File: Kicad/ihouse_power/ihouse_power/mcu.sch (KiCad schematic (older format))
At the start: 108 parts, among them J13 RJ33_Shielded, J20 Conn_02x05_Top_Bottom, J3 Conn_01x20, J4 Conn_01x20, M1 stm32f1_module, Q1 IRF7403, Q2 IRF7403, Q3 IRF7403, Q4 IRF7403, Q5 BC847, U10 MAX232, U11 L7805, U6 EL814, U7 EL814, U8 EL814, U9 24LC32

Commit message: 20190517
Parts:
- added C?: C, Capacitor_SMD:C_0805_2012Metric_Pad1.15x1.40mm_HandSolder, symbol Device:C
- added D?: D, Diode_SMD:D_MiniMELF, symbol Device:D
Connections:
- net 3VDC: now also D?.2 (A)
- net COM1: now also C?.2
- net VBAT: now also C?.1, D?.1 (K)
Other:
- moved on the sheet: BT1
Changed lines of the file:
@@
 L Device:Battery_Cell BT1
 U 1 1 5CD63D8E
-P 6150 4600
-F 0 "BT1" V 6000 4450 50  0000 L CNN
-F 1 "3V3" V 6100 4450 50  0000 L CNN
-F 2 "1220 Battery Holder:Battery_holder_1220" V 6150 4660 50  0001 C CNN
-F 3 "~" V 6150 4660 50  0001 C CNN
-	1    6150 4600
-	0    1    1    0
-$EndComp
-Wire Wire Line
-	7100 4600 6350 4600
+P 6050 4600
+F 0 "BT1" V 5900 4450 50  0000 L CNN
+F 1 "3V3" V 6000 4450 50  0000 L CNN
+F 2 "1220 Battery Holder:Battery_holder_1220" V 6050 4660 50  0001 C CNN
+F 3 "~" V 6050 4660 50  0001 C CNN
+	1    6050 4600
+	0    1    1    0
+$EndComp
 $Comp
 L Memory_EEPROM:24LC32 U9
@@
 	0    1    1    0
 $EndComp
-Wire Wire Line
-	7100 4350 6650 4350
 $Comp
 L Device:CP C11
@@
 Text HLabel 8500 5650 2    50   Output ~ 0
 ~TBCMD
-Wire Wire Line
-	7100 4450 6650 4450
 Wire Wire Line
 	7100 4850 6650 4850
@@
 Text Label 11350 4600 0    50   ~ 0
 3VDC
-Text Label 6650 4450 0    50   ~ 0
+Text Label 6800 4450 0    50   ~ 0
 3VDC
 Text Label 8350 5350 2    50   ~ 0
@@
 QCH_D3
 Wire Wire Line
-	5650 4600 6050 4600
+	5650 4600 5950 4600
 Text Label 3100 7700 2    50   ~ 0
 OPTIC_AI
@@
 Wire Wire Line
 	4250 2350 4350 2350
-Text HLabel 6650 4350 0    50   Output ~ 0
-3VDC
 $Comp
 L Connector:RJ33_Shielded J13
@@
 Text Notes 10300 9200 0    50   ~ 0
 PWM1 - WC duru pasvietimas\nPWM2 - vonios duru pasvietimas
+Text HLabel 5850 4350 0    50   Output ~ 0
+3VDC
+Wire Wire Line
+	7100 4600 6300 4600
+Wire Wire Line
+	6400 4450 6300 4450
+Wire Wire Line
+	6300 4450 6300 4600
+Connection ~ 6300 4600
+Wire Wire Line
+	6300 4600 6250 4600
+Wire Wire Line
+	5850 4350 7100 4350
+Wire Wire Line
+	7100 4450 6700 4450
+$Comp
+L Device:D D?
+U 1 1 5CEB3D8E
+P 6550 4450
+F 0 "D?" H 6500 4600 50  0000 L CNN
+F 1 "D" H 6350 4600 50  0000 L CNN
+F 2 "Diode_SMD:D_MiniMELF" H 6550 4450 50  0001 C CNN
+F 3 "~" H 6550 4450 50  0001 C CNN
+	1    6550 4450
+	1    0    0    -1
+$EndComp
+$Comp
+L Device:C C?
+U 1 1 5D3B6207
+P 6300 4850
+F 0 "C?" H 6000 4900 50  0000 L CNN
+F 1 "C" H 6000 4800 50  0000 L CNN
+F 2 "Capacitor_SMD:C_0805_2012Metric_Pad1.15x1.40mm_HandSolder" H 6338 4700 50  0001 C CNN
+F 3 "~" H 6300 4850 50  0001 C CNN
+	1    6300 4850
+	1    0    0    -1
+$EndComp
+Wire Wire Line
+	6300 4700 6300 4600
+Wire Wire Line
+	6300 5000 6300 5100
+Wire Wire Line
+	6300 5100 5650 5100
+Text Label 5650 5100 0    50   ~ 0
+COM
 $EndSCHEMATC

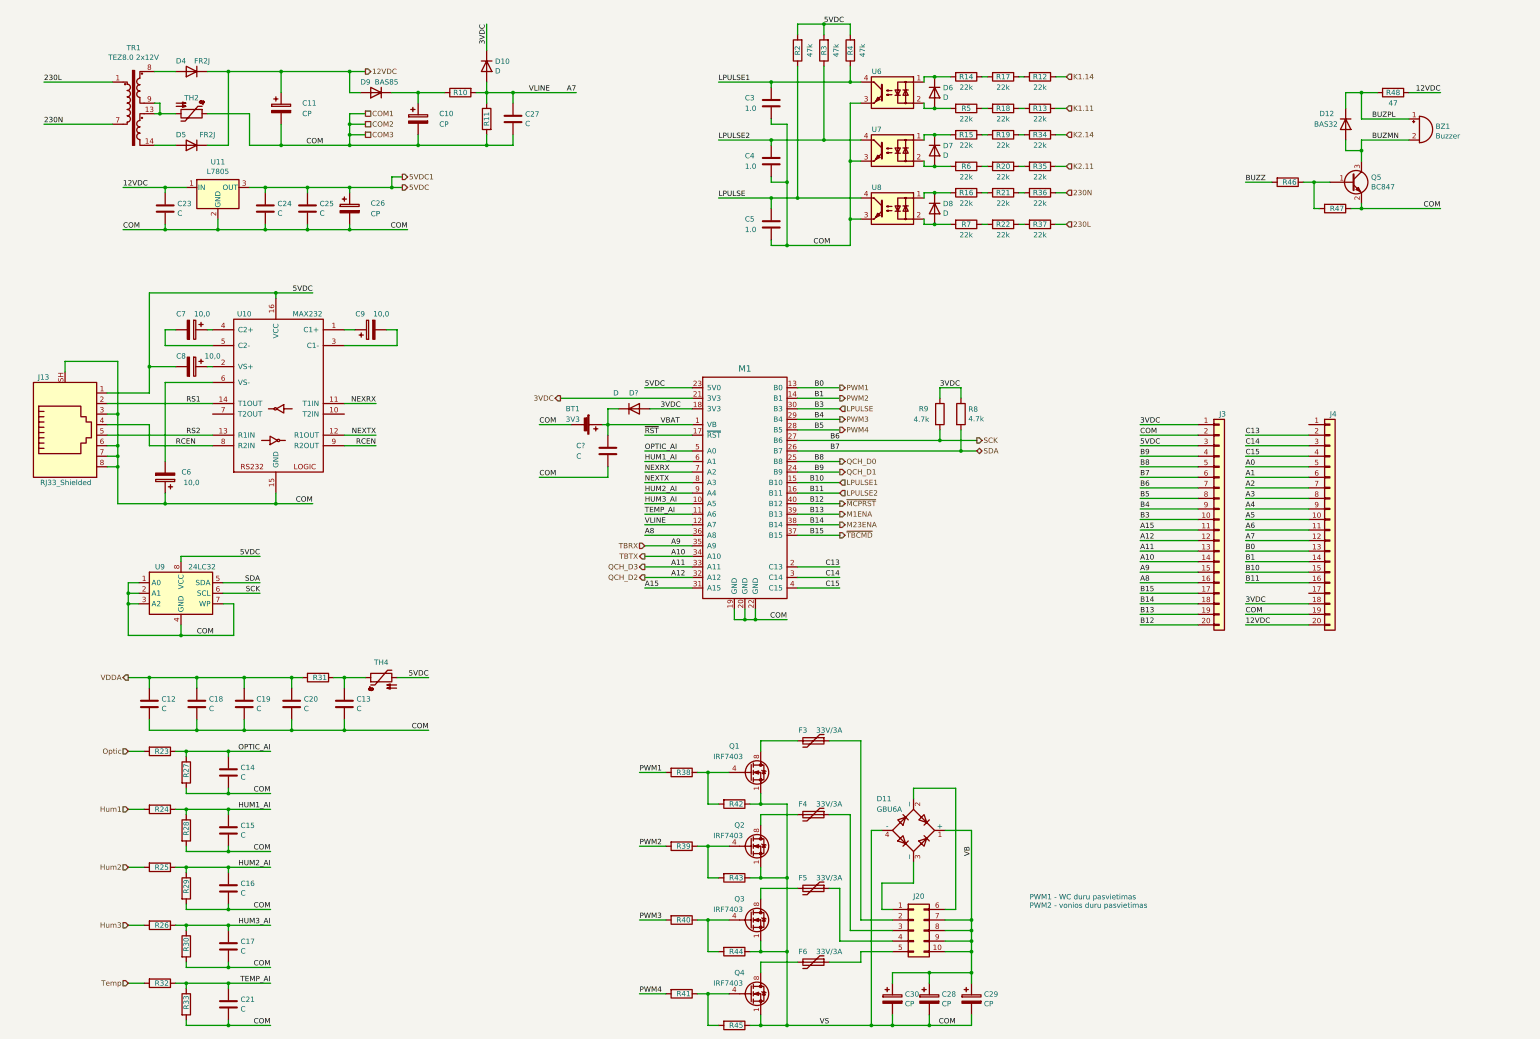
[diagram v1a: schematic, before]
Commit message: nupiesta paskirstymo dezutes schema ir pcb
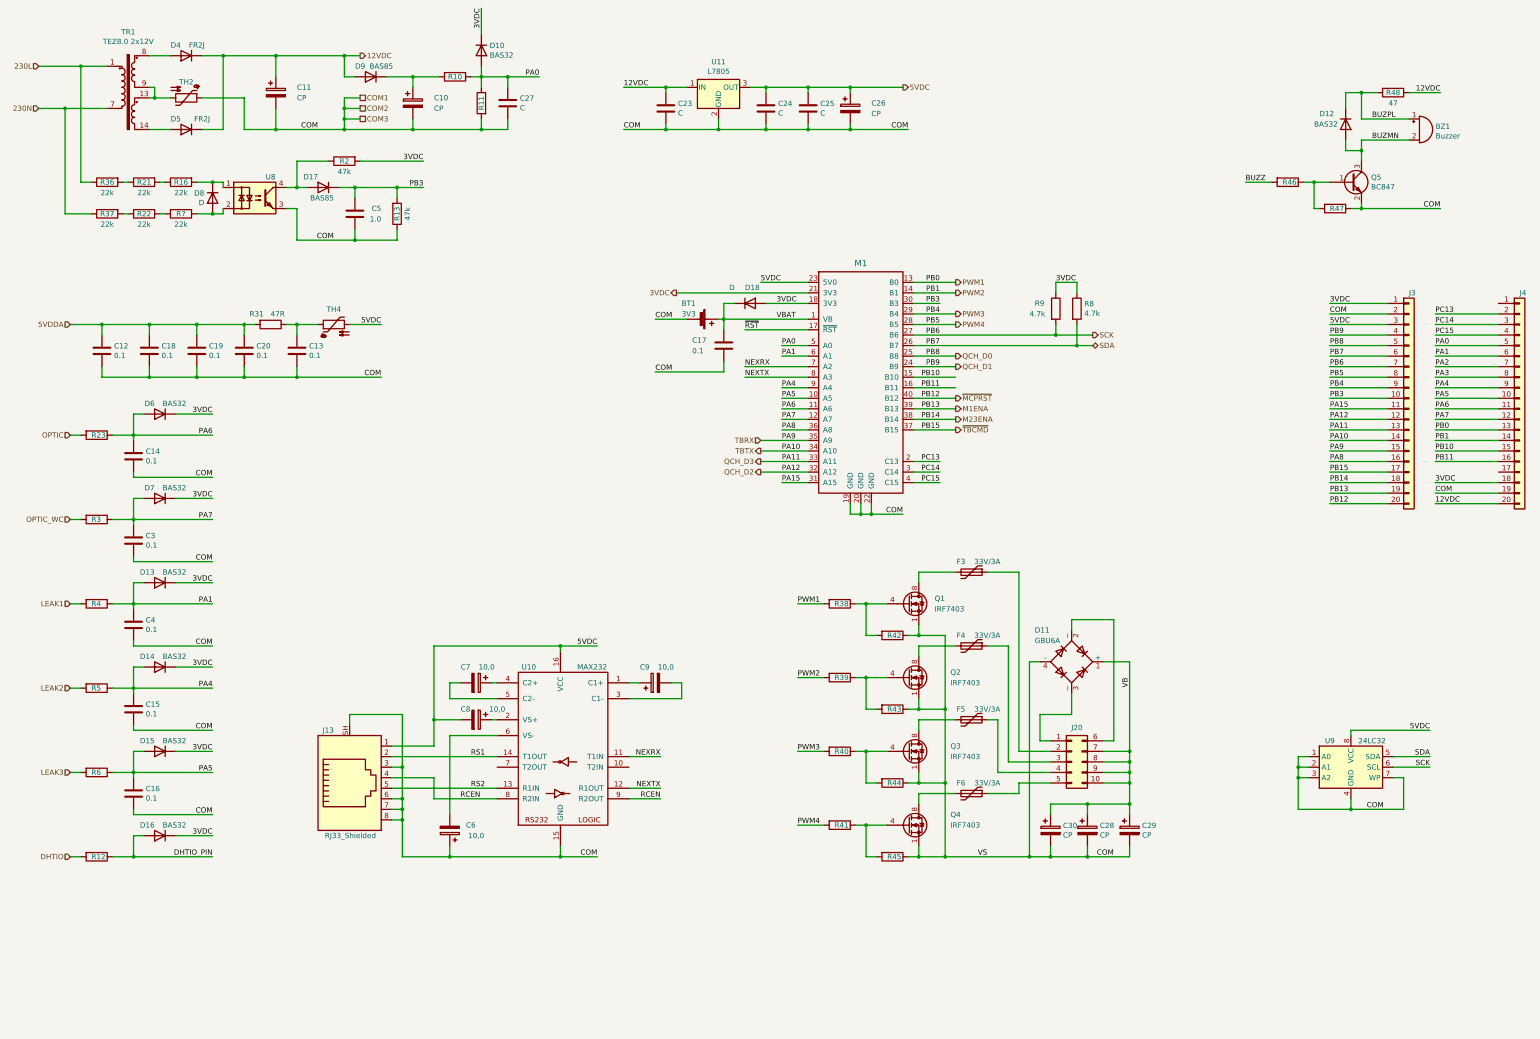
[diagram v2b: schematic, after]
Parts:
- removed C17, C21: C, Capacitor_SMD:C_0805_2012Metric_Pad1.15x1.40mm_HandSolder, symbol Device:C
- removed R14, R15, R17, R18, R19, R20, R34, R35: 22k, Resistor_SMD:R_1206_3216Metric, symbol Device:R
- removed R24, R25, R26, R32: 100, Resistor_SMD:R_0805_2012Metric_Pad1.15x1.40mm_HandSolder, symbol Device:R
- removed R27, R28, R29, R30, R33: 4.7k, Resistor_SMD:R_0805_2012Metric_Pad1.15x1.40mm_HandSolder, symbol Device:R
- removed U6, U7: EL814, Package_DIP:DIP-4_W7.62mm_LongPads, symbol Isolator:EL814
- added D13, D14, D15, D16: BAS32, Diode_SMD:D_MiniMELF, symbol Device:D
- added D17: BAS85, Diode_SMD:D_MiniMELF, symbol Device:D
- C12, C13, C14, C15, C16, C18, C19, C20: value C -> 0.1
- C17: renamed from C?; value C -> 0.1
- C3, C4: value 1.0 -> 0.1; footprint Capacitor_SMD:C_1206_3216Metric_Pad1.42x1.75mm_HandSolder -> Capacitor_SMD:C_0805_2012Metric_Pad1.15x1.40mm_HandSolder
- D10, D6, D7: value D -> BAS32
- R12, R5, R6: value 22k -> 100; footprint Resistor_SMD:R_1206_3216Metric -> Resistor_SMD:R_0805_2012Metric_Pad1.15x1.40mm_HandSolder
- R13: value 22k -> 47k; footprint Resistor_SMD:R_1206_3216Metric -> Resistor_SMD:R_0805_2012Metric_Pad1.15x1.40mm_HandSolder
- R3, R4: value 47k -> 100
- R31: value 100 -> 47R
- gave numbers to parts that had none: 1
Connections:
- net A4 is gone; now on net PA4: J4.9 (Pin_9)
- net A5 is gone; now on net PA5: J4.10 (Pin_10)
- net HUM3_AI is gone; now on net PA5: M1.10 (A5)
- net K1.11 is gone; now on net COM1: R13.1
- net TEMP_AI is gone; now on net PA6: M1.11 (A6)
- net 230L: now also R36.1; no longer R37.1
- net 230N: now also R37.1; no longer R36.1
- net 3VDC: now also D6.1 (K), D7.1 (K), R2.2, D13.1 (K), D14.1 (K), D15.1 (K), D16.1 (K)
- net 5VDC: no longer R2.2, R3.2, R4.2
- net DHTIO: now reaches R12.2
- net PB3: now reaches R13.2
- net PB3: now also C5.1, J3.10 (Pin_10), M1.30 (B3), D17.1 (K)
- net LEAK2: now reaches R5.2
- net LEAK2: no longer D6.2 (A)
- net PA4: now reaches R5.1
- net PA4: now also C15.1, M1.9 (A4), D14.2 (A)
- net LEAK3: now reaches R6.2
- net LEAK3: no longer D7.2 (A)
- net PA5: now reaches R6.1
- net PA5: now also C16.1, D15.2 (A)
- net A0 renamed PA0
- net PA0: now also C27.1, D10.2 (A), M1.5 (A0), R10.2, R11.1
- net A1 renamed PA1
- net PA1: now also C4.1, M1.6 (A1), R4.1, D13.2 (A)
- net A15 renamed PA15
- net A2 renamed PA2
- net A3 renamed PA3
- net A6 renamed PA6
- net PA6: now also C14.1, D6.2 (A), R23.1
- removed net A7: C27.1, D10.2 (A), J4.12 (Pin_12), M1.12 (A7), R10.2, R11.1
- net A8 renamed PA8
- net C13 renamed PC13
- net C14 renamed PC14
- net C15 renamed PC15
- removed net HUM1_AI: C15.1, M1.6 (A1)
- removed net HUM2_AI: C16.1, M1.9 (A4)
- net K1.14 renamed DHTIO_PIN
- net DHTIO_PIN: now also D16.2 (A)
- removed net LPULSE: C5.1, J3.10 (Pin_10), M1.30 (B3), R2.1, U8.4
- net LPULSE1 renamed PB10
- net PB10: no longer C3.1, R4.1
- net LPULSE2 renamed PB11
- net PB11: no longer C4.1, R3.1
- removed net OPTIC_AI: C14.1, M1.5 (A0), R23.1
- net Optic renamed OPTIC
- net VDDA renamed 5VDDA
- new net: D17.2 (A), R2.1, U8.4
- new net LEAK1: R4.2
- new net OPTIC_WC: R3.2
- new net PA7: C3.1, D7.2 (A), J4.12 (Pin_12), M1.12 (A7), R3.1
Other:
- note removed: "PWM1 - WC duru pasvietimas\nPWM2 - vonios duru pasvietimas"
- moved on the sheet: BT1, C10, C11, C12, C13, C14, C17, C18, C19, C20, C23, C24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

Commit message: schemos korekcijos ir ploksciu paruosimas
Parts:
- added C39: C, Capacitor_SMD:C_0805_2012Metric_Pad1.15x1.40mm_HandSolder, symbol Device:C
- added C40: 0.1, Capacitor_SMD:C_0805_2012Metric_Pad1.15x1.40mm_HandSolder, symbol Device:C
- added C41, C42: 0.1, Capacitor_SMD:C_0805_2012Metric, symbol Device:C
- added CN6, J31, J32: Conn_01x06, Connector_PinHeader_2.54mm:PinHeader_1x06_P2.54mm_Vertical, symbol Connector_Generic:Conn_01x06
- added D21: BAS85, Diode_SMD:D_MiniMELF, symbol Device:D
- added D22: BAS32, Diode_SMD:D_MiniMELF, symbol Device:D
- added M3: ev1527receiver_module, ev1527:EV1527_Receiver, symbol ihouse_power-rescue:ev1527receiver_module-ev1527_receiver_module
- added R28, R30: 4.7k, Resistor_SMD:R_0805_2012Metric, symbol Device:R
- added R32: R_PHOTO, Resistor_THT:R_Axial_DIN0204_L3.6mm_D1.6mm_P5.08mm_Horizontal, symbol Device:R_PHOTO
- added R33: R, Resistor_SMD:R_0805_2012Metric_Pad1.15x1.40mm_HandSolder, symbol Device:R
- added R34: 100, Resistor_SMD:R_0805_2012Metric_Pad1.15x1.40mm_HandSolder, symbol Device:R
- added R35: 10k, Resistor_SMD:R_0805_2012Metric_Pad1.15x1.40mm_HandSolder, symbol Device:R
- added R50: 1k, Resistor_SMD:R_0805_2012Metric_Pad1.15x1.40mm_HandSolder, symbol Device:R
- added RV4: 5k, Potentiometer_THT:Potentiometer_Piher_PT-6-V_Vertical, symbol Device:R_POT
- added SW1: BLDR, Resistor_THT:R_Axial_DIN0411_L9.9mm_D3.6mm_P15.24mm_Horizontal, symbol Switch:SW_Reed
- added SW2: USER, Resistor_THT:R_Axial_DIN0411_L9.9mm_D3.6mm_P15.24mm_Horizontal, symbol Switch:SW_Reed
- added SW3: RESET, Resistor_THT:R_Axial_DIN0411_L9.9mm_D3.6mm_P15.24mm_Horizontal, symbol Switch:SW_Reed
- added U13: LM393, Package_SO:SOIC-8_3.9x4.9mm_P1.27mm, symbol Comparator:LM393
- BT1: value 3V3 -> 3V0
- D18: value D -> BAS32
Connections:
- net DHTIO_PIN is gone; now on net PC13: D16.2 (A), R12.1
- net NEXRX is gone; now on net PA2: M1.7 (A2), U10.11 (T1IN)
- net NEXTX is gone; now on net PA3: M1.8 (A3), U10.12 (R1OUT)
- net 12VDC: no longer R48.1
- net 3VDC: now also D22.1 (K); no longer M1.18 (3V3)
- net 5VDC: now also C40.1, J31.3 (Pin_3), M3.6 (VCC)
- net BUZPL: now also R48.1; no longer R48.2
- net COM1: now also C40.2, J31.5 (Pin_5), J31.6 (Pin_6), M3.7 (COM); no longer Q5.2 (E), R47.1
- net OPTIC: now also J31.4 (Pin_4)
- net PA8: now also D22.2 (A), R50.1
- net PB10: now also M3.3 (CH3)
- net PB11: now also M3.2 (CH4)
- net PWM1: now also J3.9 (Pin_9), M1.29 (B4); no longer J4.13 (Pin_13), M1.13 (B0)
- net PWM2: now also J3.8 (Pin_8), M1.28 (B5); no longer J4.14 (Pin_14), M1.14 (B1)
- net PWM3: now also J4.13 (Pin_13), M1.13 (B0); no longer J3.9 (Pin_9), M1.29 (B4)
- net PWM4: now also J4.14 (Pin_14), M1.14 (B1); no longer J3.8 (Pin_8), M1.28 (B5)
- net VBAT: now also D21.1 (K); no longer BT1.1 (+)
- net ~RST: now also J31.2 (Pin_2)
- net BUZZ: no longer names the net of R46.2
- net BUZZ: now also J32.1 (Pin_1)
- net QCH_D0 renamed PB8
- net PB8: now also M3.5 (CH1)
- net QCH_D1 renamed PB9
- net PB9: now also M3.4 (CH2)
- net QCH_D2 renamed PA12
- net QCH_D3 renamed PA11
- net PA11: now also J31.1 (Pin_1)
- removed net RCEN: J13.4, U10.8 (R2IN), U10.9 (R2OUT)
- net SCK renamed SCL
- new net: J13.4, R50.2
- new net: BT1.1 (+), D21.2 (A)
- new net: CN6.3 (Pin_3), R28.2, SW1.2
- new net: J32.2 (Pin_2), SW3.2
- new net: R32.2, R33.2, U13.3 (+)
- new net: J32.4 (Pin_4), R35.2, U13.1
- new net: C42.1, RV4.2, U13.2 (-)
- new net: R34.2, RV4.3
- new net 3V@1: CN6.1 (Pin_1), CN6.2 (Pin_2), R30.2, SW1.1
- new net 5V@1: C41.1, J32.3 (Pin_3), R33.1, R34.1, R35.1, R48.2, U13.8 (V+)
- new net COM@1: C39.2, C41.2, C42.2, CN6.5 (Pin_5), CN6.6 (Pin_6), J32.5 (Pin_5), J32.6 (Pin_6), Q5.2 (E), R28.1, R32.1, R47.1, RV4.1, SW2.1, SW3.1, U13.4 (V-), U13.5 (+), U13.6 (_)
- new net PB2: C39.1, CN6.4 (Pin_4), R30.1, SW2.2
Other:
- note added: "3VDC"
- note added: "5VDC"
- note added: "BLDR"
- note added: "BUZZ"
- note added: "GND"
- note added: "OPTIC"
- note added: "USER"
- note added: "~RST"
- moved on the sheet: BT1, BZ1, C17, C23, C24, C25, C26, C28, C29, C30, C6, C7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

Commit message: schemos ir pcb ruosimas
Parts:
- removed C12, C18, C19, C20: 0.1, Capacitor_SMD:C_0805_2012Metric_Pad1.15x1.40mm_HandSolder, symbol Device:C
- removed D8: D, Diode_SMD:D_MiniMELF, symbol Device:D
- removed R16, R21, R22, R36, R37, R7: 22k, Resistor_SMD:R_1206_3216Metric, symbol Device:R
- removed TH4: Thermistor_PTC, Resistor_SMD:R_1206_3216Metric_Pad1.42x1.75mm_HandSolder, symbol Device:Thermistor_PTC
- removed U8: EL814, Package_DIP:DIP-4_W7.62mm_LongPads, symbol Isolator:EL814
- C23, C24, C25: value C -> 0.1
- C26: value CP -> 100x16V
- C5: value 1.0 -> 10n; footprint Capacitor_SMD:C_1206_3216Metric_Pad1.42x1.75mm_HandSolder -> Capacitor_SMD:C_0805_2012Metric
- D17: value BAS85 -> BAS32
- R13: value 47k -> 10k
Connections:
- net 3V@1: no longer CN6.2 (Pin_2)
- net 3VDC: now also D17.1 (K); no longer R2.2
- net 5VDC: now also R31.1
- net 5VDDA: now also C13.1
- net PB3: now also D17.2 (A), R2.2; no longer D17.1 (K)
- net LPULSE: now reaches D4.2 (A), TR1.8
- net LPULSE: now also R2.1
- net COM1 renamed COM
- net OPTIC_WC renamed OPTICWC
- net PB2: no longer names the net of C39.1, CN6.4 (Pin_4), R30.1, SW2.2
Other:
- note added: "KEY\n"
- moved on the sheet: BZ1, C11, C13, C14, C15, C16, C23, C24, C25, C26, C3, C39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
